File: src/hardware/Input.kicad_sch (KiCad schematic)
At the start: 9 parts, among them J601 CONTROLS, SW201 TILT, U601 74HC165, U602 74HC165

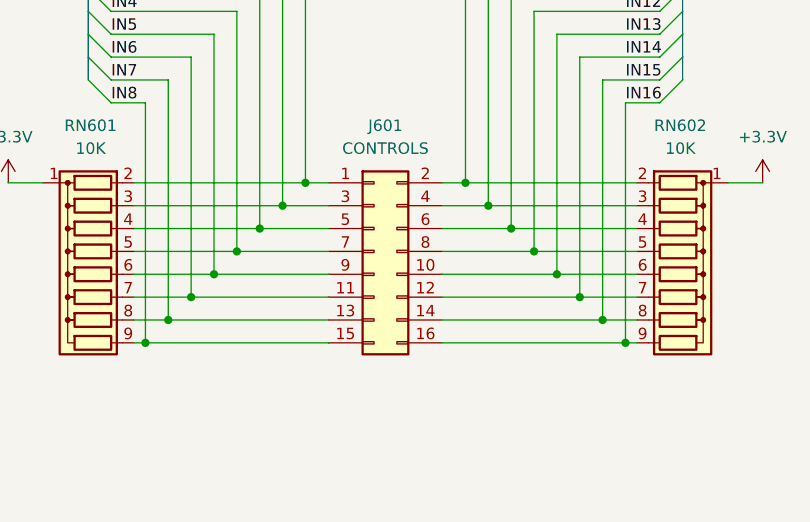
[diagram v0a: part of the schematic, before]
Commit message: Added silkscreen idents & fixed missing gnd pin on input hdr
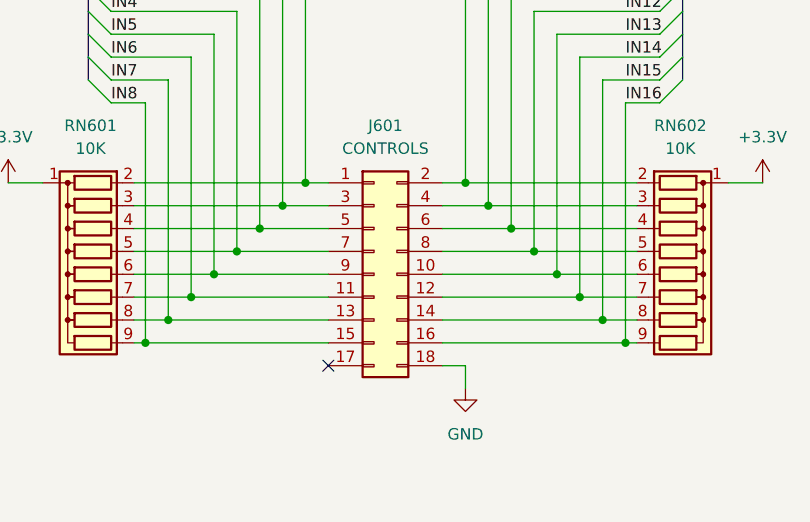
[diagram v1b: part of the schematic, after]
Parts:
- removed J601: CONTROLS, Connector_PinHeader_2.54mm:PinHeader_2x08_P2.54mm_Vertical, symbol Connector_Generic:Conn_02x08_Odd_Even
- added J601: CONTROLS, Connector_PinHeader_2.54mm:PinHeader_2x09_P2.54mm_Vertical, symbol Connector_Generic:Conn_02x09_Odd_Even
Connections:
- net GND: now also J601.18 (Pin_18)
- net IN1: now also J601.1 (Pin_1)
- net IN10: now also J601.4 (Pin_4)
- net IN11: now also J601.6 (Pin_6)
- net IN12: now also J601.8 (Pin_8)
- net IN13: now also J601.10 (Pin_10)
- net IN14: now also J601.12 (Pin_12)
- net IN15: now also J601.14 (Pin_14)
- net IN16: now also J601.16 (Pin_16)
- net IN2: now also J601.3 (Pin_3)
- net IN3: now also J601.5 (Pin_5)
- net IN4: now also J601.7 (Pin_7)
- net IN5: now also J601.9 (Pin_9)
- net IN6: now also J601.11 (Pin_11)
- net IN7: now also J601.13 (Pin_13)
- net IN8: now also J601.15 (Pin_15)
- net IN9: now also J601.2 (Pin_2)
- no-connect marks 2 -> 3

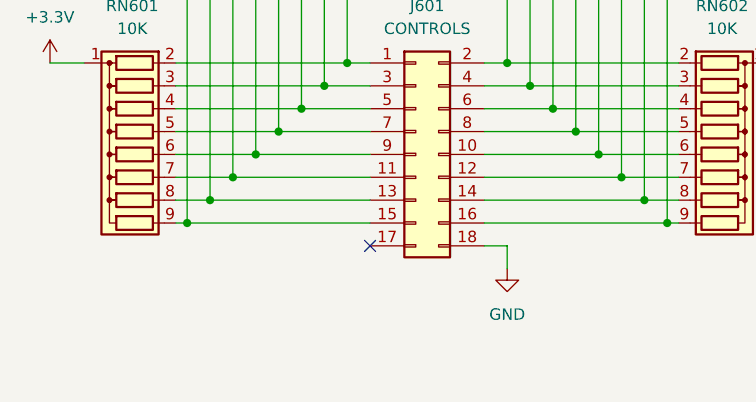
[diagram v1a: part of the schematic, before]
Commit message: Added second gnd to input hdr
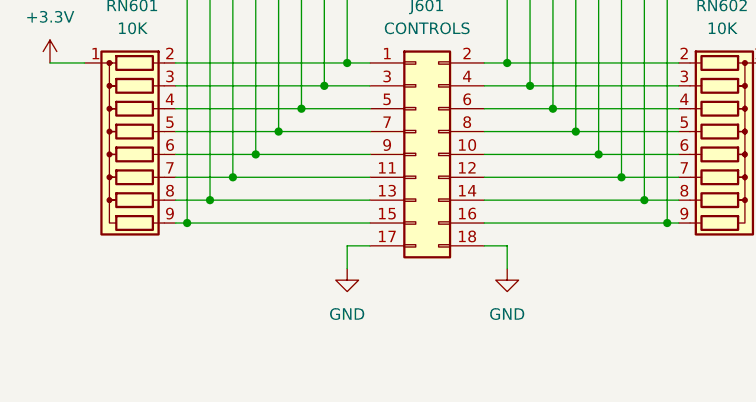
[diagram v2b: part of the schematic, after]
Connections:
- net GND: now also J601.17 (Pin_17)
- no-connect marks 3 -> 2
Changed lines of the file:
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@@
   )
   (no_connect (at 266.7 83.82))
-  (no_connect (at 68.58 113.03))
   (no_connect (at 182.88 83.82))
   (bus_entry (at 44.45 73.66) (size -2.54 -2.54)
@@
     (stroke (width 0) (type default))
   )
+  (wire (pts (xy 66.04 113.03) (xy 66.04 115.57))
+    (stroke (width 0) (type default))
+  )
   (bus (pts (xy 148.59 88.9) (xy 148.59 91.44))
     (stroke (width 0) (type default))
@@
   )
   (wire (pts (xy 88.9 97.79) (xy 81.28 97.79))
+    (stroke (width 0) (type default))
+  )
+  (wire (pts (xy 68.58 113.03) (xy 66.04 113.03))
     (stroke (width 0) (type default))
   )
@@
         )
       )
+    )
+  )
+  (symbol (lib_id "power:GND") (at 66.04 115.57 0) (unit 1)
+    (in_bom yes) (on_board yes) (dnp no) (fields_autoplaced)
+    (property "Reference" "#PWR?" (at 66.04 121.92 0)
+      (effects (font (size 1.27 1.27)) hide)
+    )
+    (property "Value" "GND" (at 66.04 120.65 0)
+      (effects (font (size 1.27 1.27)))
+    )
+    (property "Footprint" "" (at 66.04 115.57 0)
+      (effects (font (size 1.27 1.27)) hide)
+    )
+    (property "Datasheet" "" (at 66.04 115.57 0)
+      (effects (font (size 1.27 1.27)) hide)
+    )
+    (pin "1")
+    (instances
+      (project "jcap"
+        (path "/7fc25e9e-3600-419b-89ef-b962e4e374c1/203ea849-2dbb-4e64-89c6-7fa05a05e11f"
+          (reference "#PWR?") (unit 1)
+        )
+        (path "/7fc25e9e-3600-419b-89ef-b962e4e374c1/86e6f384-c422-400d-8407-2294b351ad7e"
+          (reference "#PWR0612") (unit 1)
+        )
+      )
